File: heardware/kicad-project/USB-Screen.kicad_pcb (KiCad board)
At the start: 2 copper layers, 32 x 34 mm, 23 parts, among them J1 USB_B_Micro, J2 Conn_01x04, Q1 NPN, U1 ZJY154T-PG04, U2 CH551, U3 SC662

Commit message: 二极管换成小封装的
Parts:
- removed the R2 at (117.3, 102.2)
- D4, D5: value SS14 -> SD103AWS; footprint Diode_SMD:D_SMA -> Diode_SMD:D_SOD-323
- moved D5 3.17 mm to (114.1, 90.5), turned to 90 degrees
- moved D4 2.54 mm to (116.0, 90.5), turned to 90 degrees
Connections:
- J1 pad 4: Net-(J1-Pad4) -> (no net)
- U2 pad 4: Net-(U2-Pad4) -> (no net)
- U2 pad 6: Net-(U2-Pad6) -> (no net)
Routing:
- net /DC: track 9.80 -> 3.79 mm
- net /SDA: track 15.7 -> 10.5 mm
- net /CS: track 10.1 -> 14.1 mm
- net /SCL: track 9.27 -> 10.8 mm
- net Net-(D5-Pad1): track 3.42 -> 2.11 mm
- net Net-(D4-Pad1): track 3.12 -> 2.14 mm
- net (no net): vias 0 -> 5

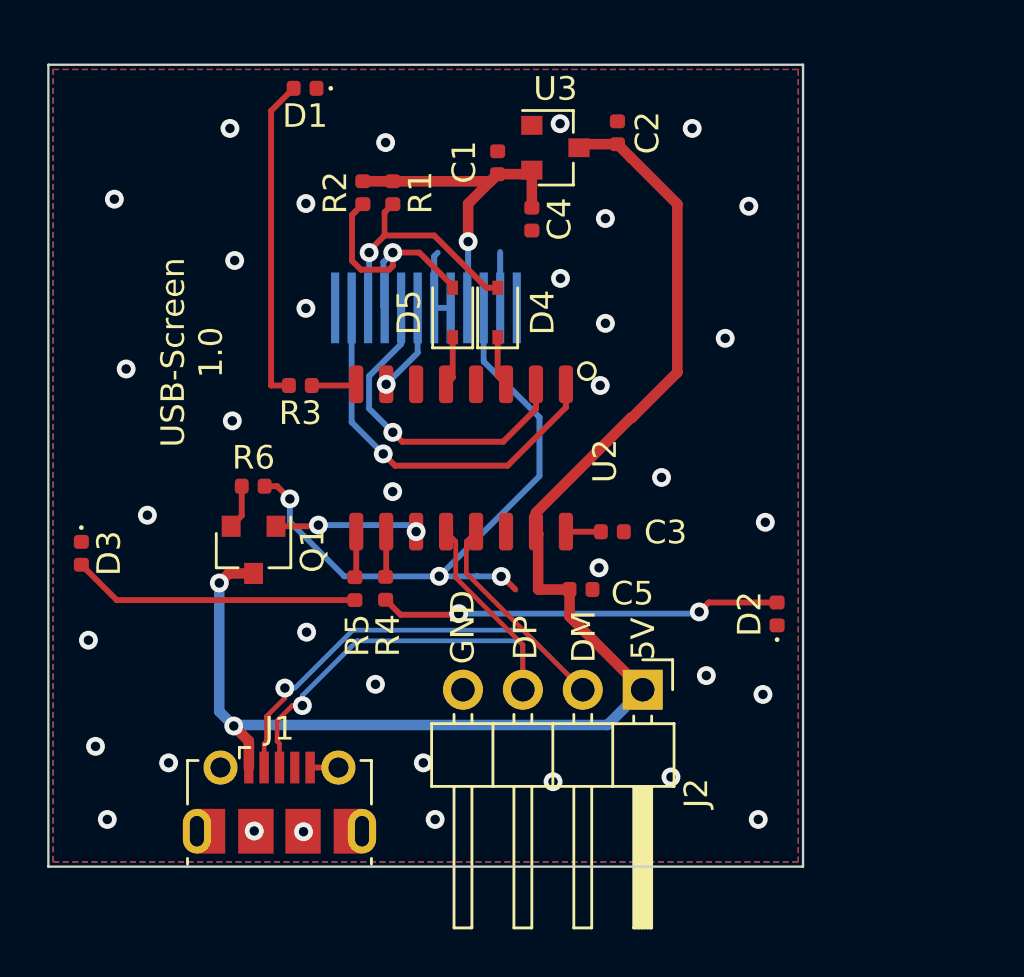
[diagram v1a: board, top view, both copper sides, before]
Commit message: 更改pcb布局
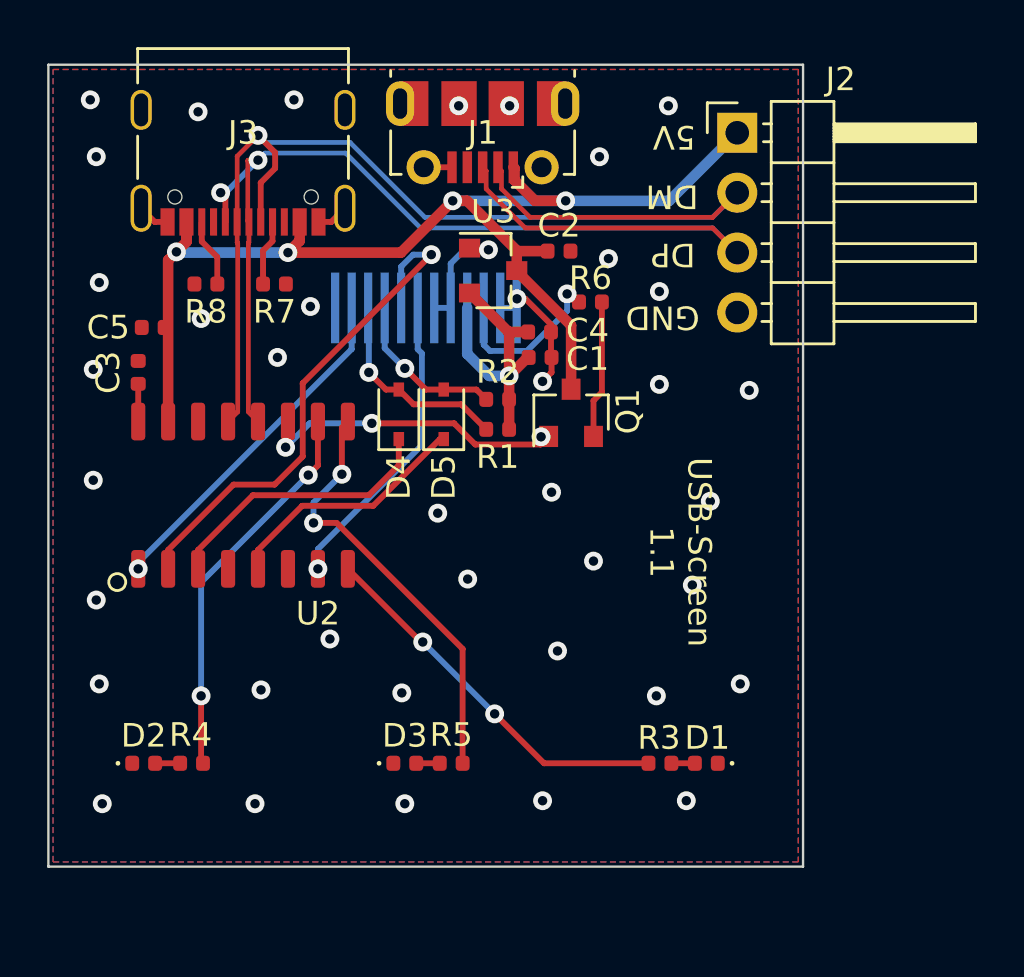
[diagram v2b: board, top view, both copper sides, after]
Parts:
- added J3: USB_C_Receptacle_USB2.0, Connector_USB:USB_C_Receptacle_Palconn_UTC16-G, F.Cu at (105.3, 84.2)
- added R7: 5.1K, Resistor_SMD:R_0402_1005Metric, F.Cu at (106.6, 89.3)
- added R8: 5.1K, Resistor_SMD:R_0402_1005Metric, F.Cu at (103.7, 89.3)
- D4, D5: value SD103AWS -> 1n4148
- moved D1 33.3 mm to (124.9, 109.6)
- moved J1 29.7 mm to (115.4, 82.9), turned to 180 degrees
- moved D2 27.6 mm to (101.0, 109.6), turned to 0 degrees
- moved J2 24.0 mm to (126.2, 82.9), turned to 0 degrees
- moved R3 22.1 mm to (122.9, 109.6), turned to 0 degrees
- moved C5 21.3 mm to (101.4, 91.1), turned to 180 degrees
- moved C3 21.2 mm to (100.8, 93.0), turned to 270 degrees
- moved D3 16.3 mm to (112.1, 109.6), turned to 0 degrees
- moved R6 16.3 mm to (120.0, 90.1), turned to 0 degrees
- moved Q1 14.7 mm to (119.2, 94.8), turned to 90 degrees
- moved R4 11.1 mm to (103.1, 109.6), turned to 180 degrees
- moved R1 11.0 mm to (116.0, 95.5), turned to 180 degrees
- moved R2 10.5 mm to (116.0, 94.2), turned to 0 degrees
- moved U2 9.34 mm to (105.3, 98.1), turned to 90 degrees
- moved R5 8.45 mm to (114.1, 109.6), turned to 180 degrees
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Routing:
- net /USB_D+: track 24.1 -> 50.1 mm, vias 1 -> 2
- net /USB_D-: track 27.3 -> 51.0 mm
- net /KEDA: track 27.1 -> 7.27 mm, vias 3 -> 1
- net /LED3: track 1.96 -> 18.9 mm, vias 0 -> 2
- net Net-(D2-Pad2): track 17.1 -> 1.06 mm, vias 2 -> 0
- net /LED2: track 1.93 -> 16.6 mm, vias 0 -> 2
- net /LED1: track 1.91 -> 16.2 mm, vias 0 -> 2
- net Net-(D1-Pad2): track 13.8 -> 1.00 mm
- net Net-(D3-Pad2): track 12.2 -> 1.00 mm
- net Net-(D4-Pad1): track 2.14 -> 11.9 mm
- net /DC: track 3.79 -> 13.0 mm
- net Net-(D5-Pad1): track 2.11 -> 10.6 mm
- net /CS: track 14.1 -> 22.2 mm
- net +5V: track 59.5 -> 51.8 mm, vias 2 -> 4
- net /PWM: track 6.08 -> 13.6 mm, vias 2 -> 3
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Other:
- board text added: "USB-Screen 1.1"
- board text removed: "USB-Screen 1.0"

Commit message: 三个led改成按键
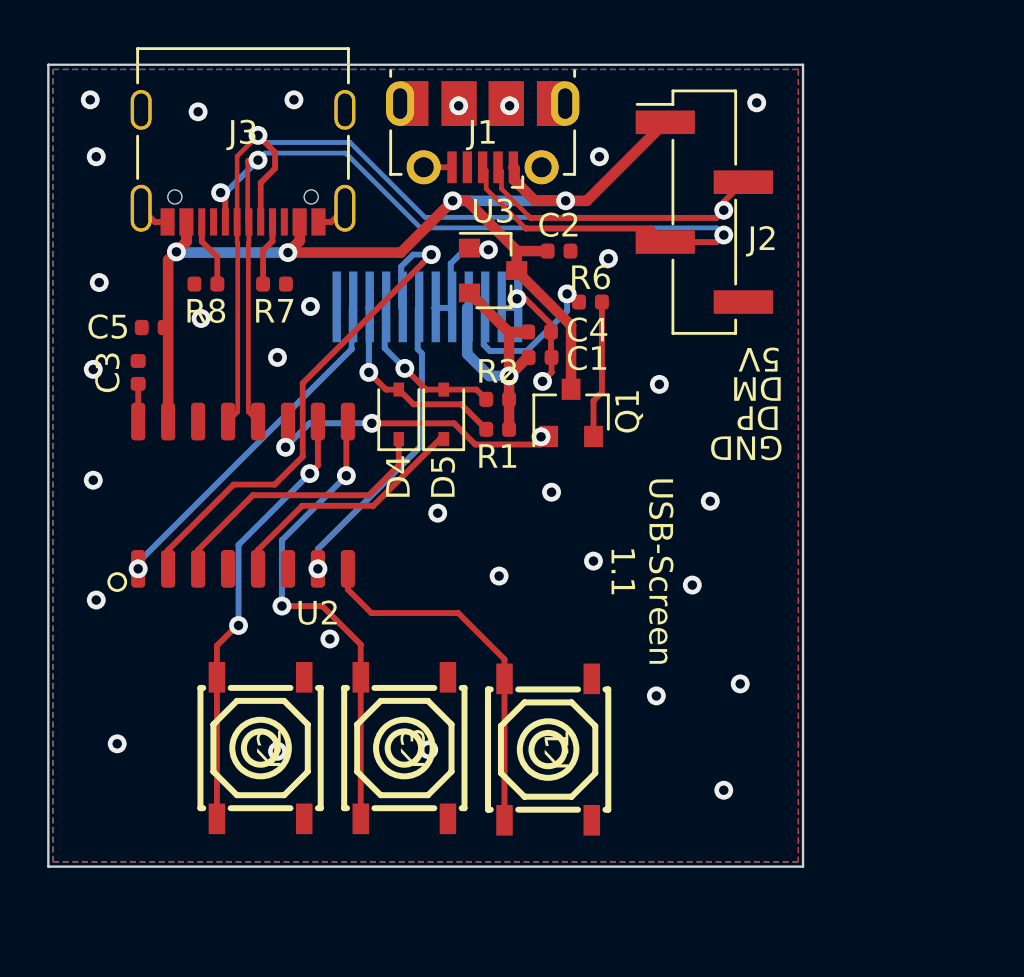
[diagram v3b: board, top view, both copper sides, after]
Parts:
- removed D1, D2, D3: LED, LED_SMD:LED_0402_1005Metric
- removed R3, R4, R5: 33R, Resistor_SMD:R_0402_1005Metric
- added K1: SW_4*4mm, USB-Screen:SW_4mm_4mm, F.Cu at (118.1, 109.0)
- added K2: SW_4*4mm, USB-Screen:SW_4mm_4mm, F.Cu at (105.9, 109.0)
- added K3: SW_4*4mm, USB-Screen:SW_4mm_4mm, F.Cu at (112.0, 109.0)
- J2: footprint Connector_PinHeader_2.54mm:PinHeader_1x04_P2.54mm_Horizontal -> Connector_PinHeader_2.54mm:PinHeader_1x04_P2.54mm_Vertical_SMD_Pin1Left
- moved J2 3.64 mm to (124.8, 86.3)
- moved U1 0.08 mm to (113.1, 96.9)
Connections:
- U2 pad 10: /LED2 -> /K2
- U2 pad 8: /LED1 -> /K1
- U2 pad 9: /LED3 -> /K3
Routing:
- net /K3: track 0.00 -> 20.4 mm, vias 0 -> 2
- net /LED3: track 18.9 -> 0.00 mm, vias 2 -> 0
- net /K2: track 0.00 -> 18.7 mm, vias 0 -> 2
- net /LED2: track 16.6 -> 0.00 mm, vias 2 -> 0
- net /LED1: track 16.2 -> 0.00 mm, vias 2 -> 0
- net /K1: track 0.00 -> 15.6 mm
- net +5V: track 51.8 -> 49.0 mm
- net /USB_D+: track 50.1 -> 48.6 mm, vias 2 -> 3
- net Net-(D2-Pad2): track 1.06 -> 0.00 mm
- net Net-(D3-Pad2): track 1.00 -> 0.00 mm
- net Net-(D1-Pad2): track 1.00 -> 0.00 mm
- net /USB_D-: track 51.0 -> 50.8 mm, vias 1 -> 2
- net GND: vias 40 -> 33

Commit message: 添加俩个3D封装
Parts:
- J3: footprint Connector_USB:USB_C_Receptacle_Palconn_UTC16-G -> Connector_USB:USB_C_Receptacle_Steady_UTC16-G
- K1: footprint USB-Screen:SW_4mm_4mm -> Button_Switch_SMD:SW_Push_1P1T_NO_4x4mm_H2.0mm
- K2: renamed from K3; footprint USB-Screen:SW_4mm_4mm -> Button_Switch_SMD:SW_Push_1P1T_NO_4x4mm_H2.0mm
- K3: renamed from K2; footprint USB-Screen:SW_4mm_4mm -> Button_Switch_SMD:SW_Push_1P1T_NO_4x4mm_H2.0mm
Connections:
- J1 pad 4: (no net) -> Net-(J1-Pad4)
- J3 pad A8: (no net) -> Net-(J3-PadA8)
- J3 pad B8: (no net) -> Net-(J3-PadB8)
- K1 pad 2: /K1 -> GND
- K2 pad 1: /K3 -> /K2
- K2 pad 2: /K3 -> GND
- K3 pad 1: /K2 -> /K3
- K3 pad 2: /K2 -> GND
- U2 pad 10: /K2 -> /K3
- U2 pad 4: (no net) -> Net-(U2-Pad4)
- U2 pad 6: (no net) -> Net-(U2-Pad6)
- U2 pad 9: /K3 -> /K2
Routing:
- net /K3: track 20.4 -> 18.7 mm
- net /K2: track 18.7 -> 20.4 mm
